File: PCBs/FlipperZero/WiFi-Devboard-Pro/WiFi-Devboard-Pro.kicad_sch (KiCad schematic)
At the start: 8 parts

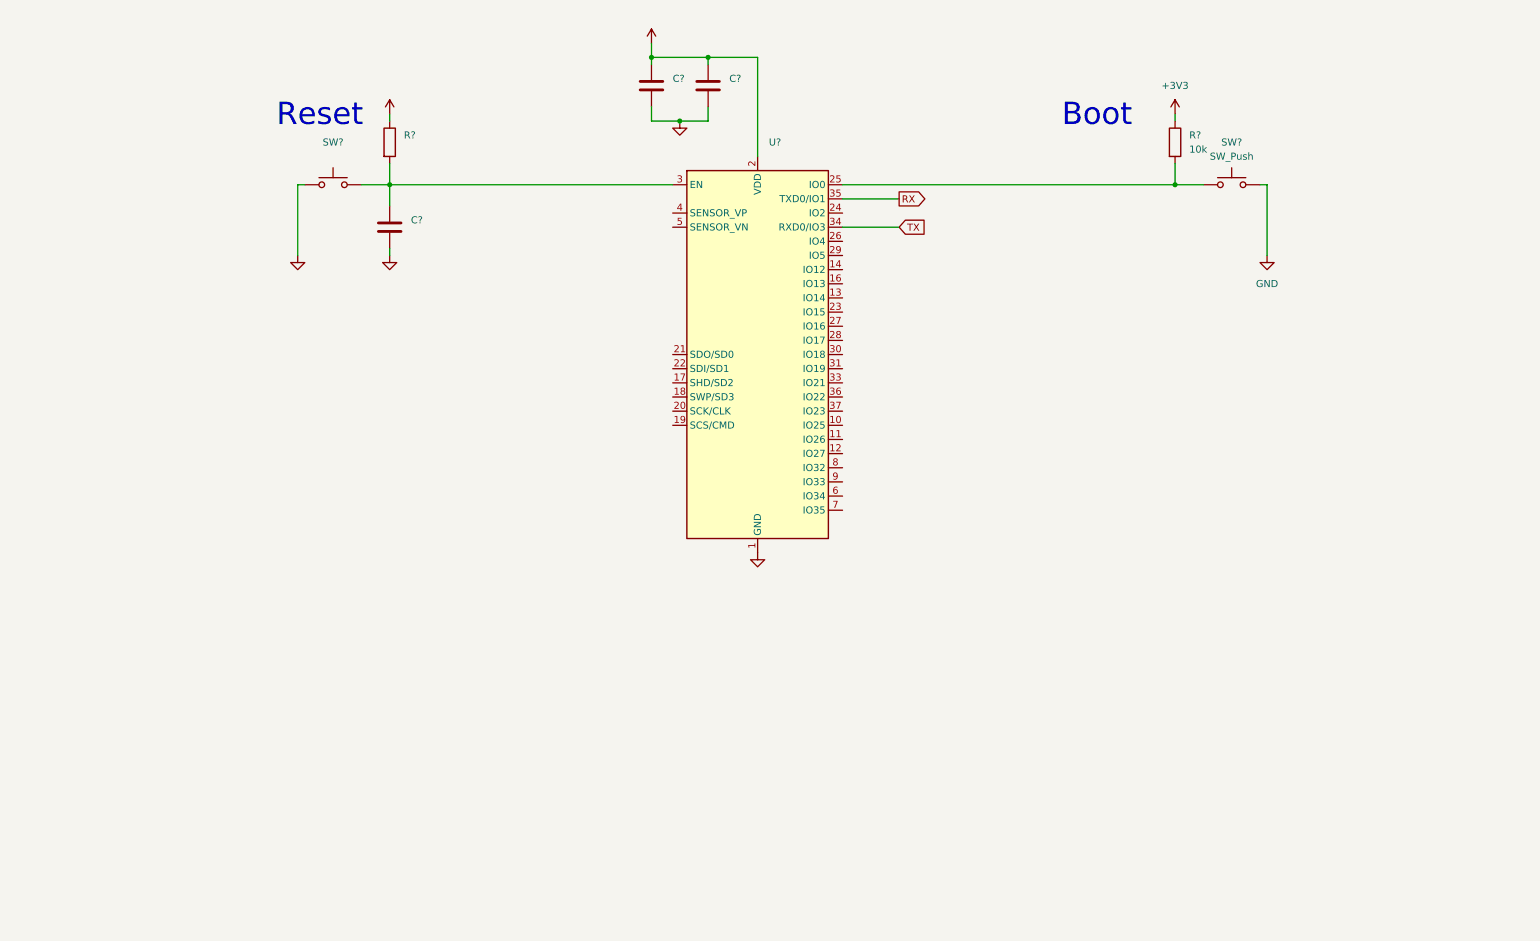
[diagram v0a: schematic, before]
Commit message: add references, edit devboard pro schematic, sd card, pin headers
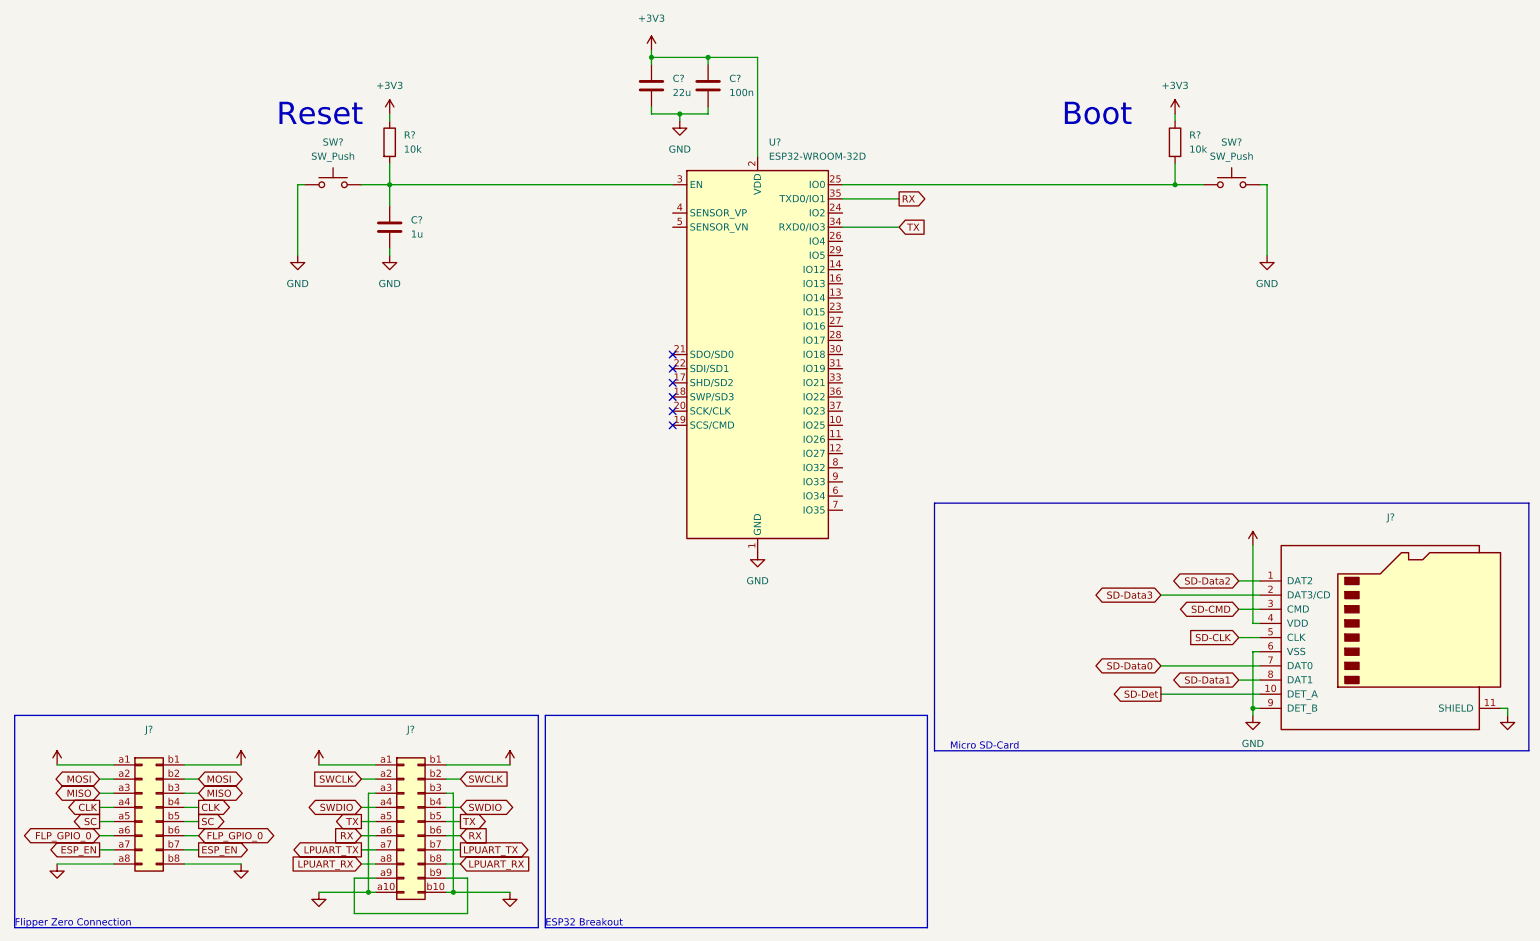
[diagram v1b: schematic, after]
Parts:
- added J?: (no value), symbol Connector_Generic:Conn_02x10_Row_Letter_First
- added J?: (no value), symbol Connector_Generic:Conn_02x08_Row_Letter_First
- added J?: (no value), symbol Connector:Micro_SD_Card_Det
- C?: value (none) -> 22u
- C?: value (none) -> 100n
- C?: value (none) -> 1u
- R?: value (none) -> 10k
- SW?: value (none) -> SW_Push
- U?: value (none) -> ESP32-WROOM-32D; footprint (none) -> RF_Module:ESP32-WROOM-32
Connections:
- net +3V3: now also J?.4 (VDD), J?.a1 (Pin_a1), J?.b1 (Pin_b1)
- net GND: now also J?.11 (SHIELD), J?.6 (VSS), J?.9 (DET_B), J?.a10 (Pin_a10), J?.a3 (Pin_a3), J?.a8 (Pin_a8), J?.b10 (Pin_b10), J?.b3 (Pin_b3), J?.b8 (Pin_b8)
- net RX: now also J?.a6 (Pin_a6), J?.b6 (Pin_b6)
- net TX: now also J?.a5 (Pin_a5), J?.b5 (Pin_b5)
- new net: J?.a9 (Pin_a9), J?.b9 (Pin_b9)
- new net +5V: J?.a1 (Pin_a1), J?.b1 (Pin_b1)
- new net CLK: J?.a4 (Pin_a4), J?.b4 (Pin_b4)
- new net ESP_EN: J?.a7 (Pin_a7), J?.b7 (Pin_b7)
- new net FLP_GPIO_0: J?.a6 (Pin_a6), J?.b6 (Pin_b6)
- new net LPUART_RX: J?.a8 (Pin_a8), J?.b8 (Pin_b8)
- new net LPUART_TX: J?.a7 (Pin_a7), J?.b7 (Pin_b7)
- new net MISO: J?.a3 (Pin_a3), J?.b3 (Pin_b3)
- new net MOSI: J?.a2 (Pin_a2), J?.b2 (Pin_b2)
- new net SC: J?.a5 (Pin_a5), J?.b5 (Pin_b5)
- new net SD-CLK: J?.5 (CLK)
- new net SD-CMD: J?.3 (CMD)
- new net SD-Data0: J?.7 (DAT0)
- new net SD-Data1: J?.8 (DAT1)
- new net SD-Data2: J?.1 (DAT2)
- new net SD-Data3: J?.2 (DAT3/CD)
- new net SD-Det: J?.10 (DET_A)
- new net SWCLK: J?.a2 (Pin_a2), J?.b2 (Pin_b2)
- new net SWDIO: J?.a4 (Pin_a4), J?.b4 (Pin_b4)
- no-connect marks 0 -> 6
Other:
- note added: "ESP32 Breakout"
- note added: "Flipper Zero Connection"
- note added: "Micro SD-Card"

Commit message: Add mosfet and transistors for power mgmt
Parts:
- added IC? (x4): DMP1045U-7, SOT96P240X120-3N, symbol SamacSys_Parts:DMP1045U-7
- added U? (x4): MMDT2907A-7-F, SOT65P210X110-6N, symbol SamacSys_Parts:MMDT2907A-7-F
- J?: value (none) -> Conn_02x10_Row_Letter_First
- J?: value (none) -> Conn_02x08_Row_Letter_First
- J?: value (none) -> Micro_SD_Card_Det; footprint (none) -> Connector_Card:microSD_HC_Hirose_DM3D-SF

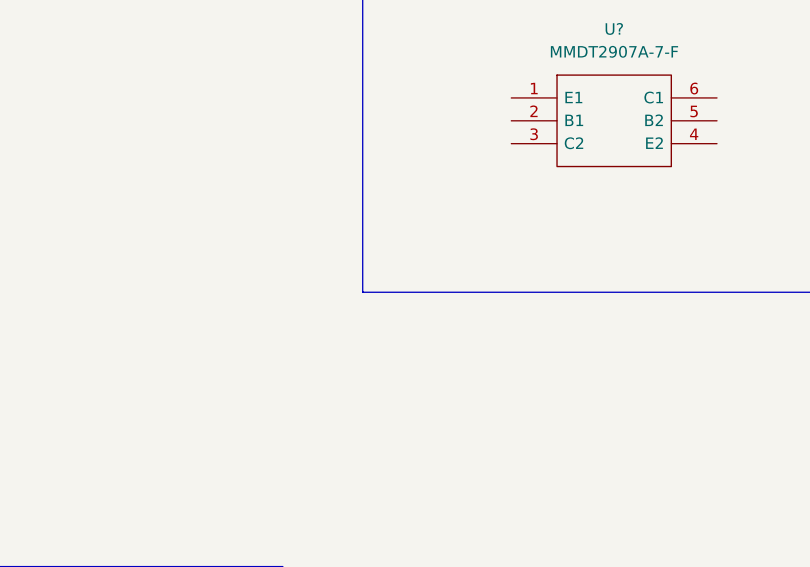
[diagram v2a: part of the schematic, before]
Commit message: Add label for power management
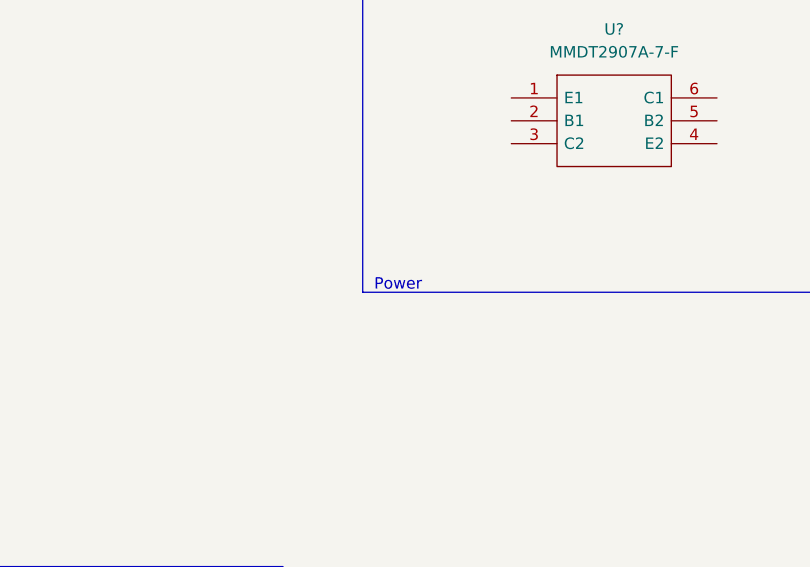
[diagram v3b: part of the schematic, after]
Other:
- note added: "Power"
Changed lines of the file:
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@@
     (effects (font (size 4 4)) (justify left bottom))
+  )
+  (text "Power" (at 294.64 90.17 0)
+    (effects (font (size 1.27 1.27)) (justify left bottom))
   )
   (text "Flipper Zero Connection" (at 12.7 196.85 0)

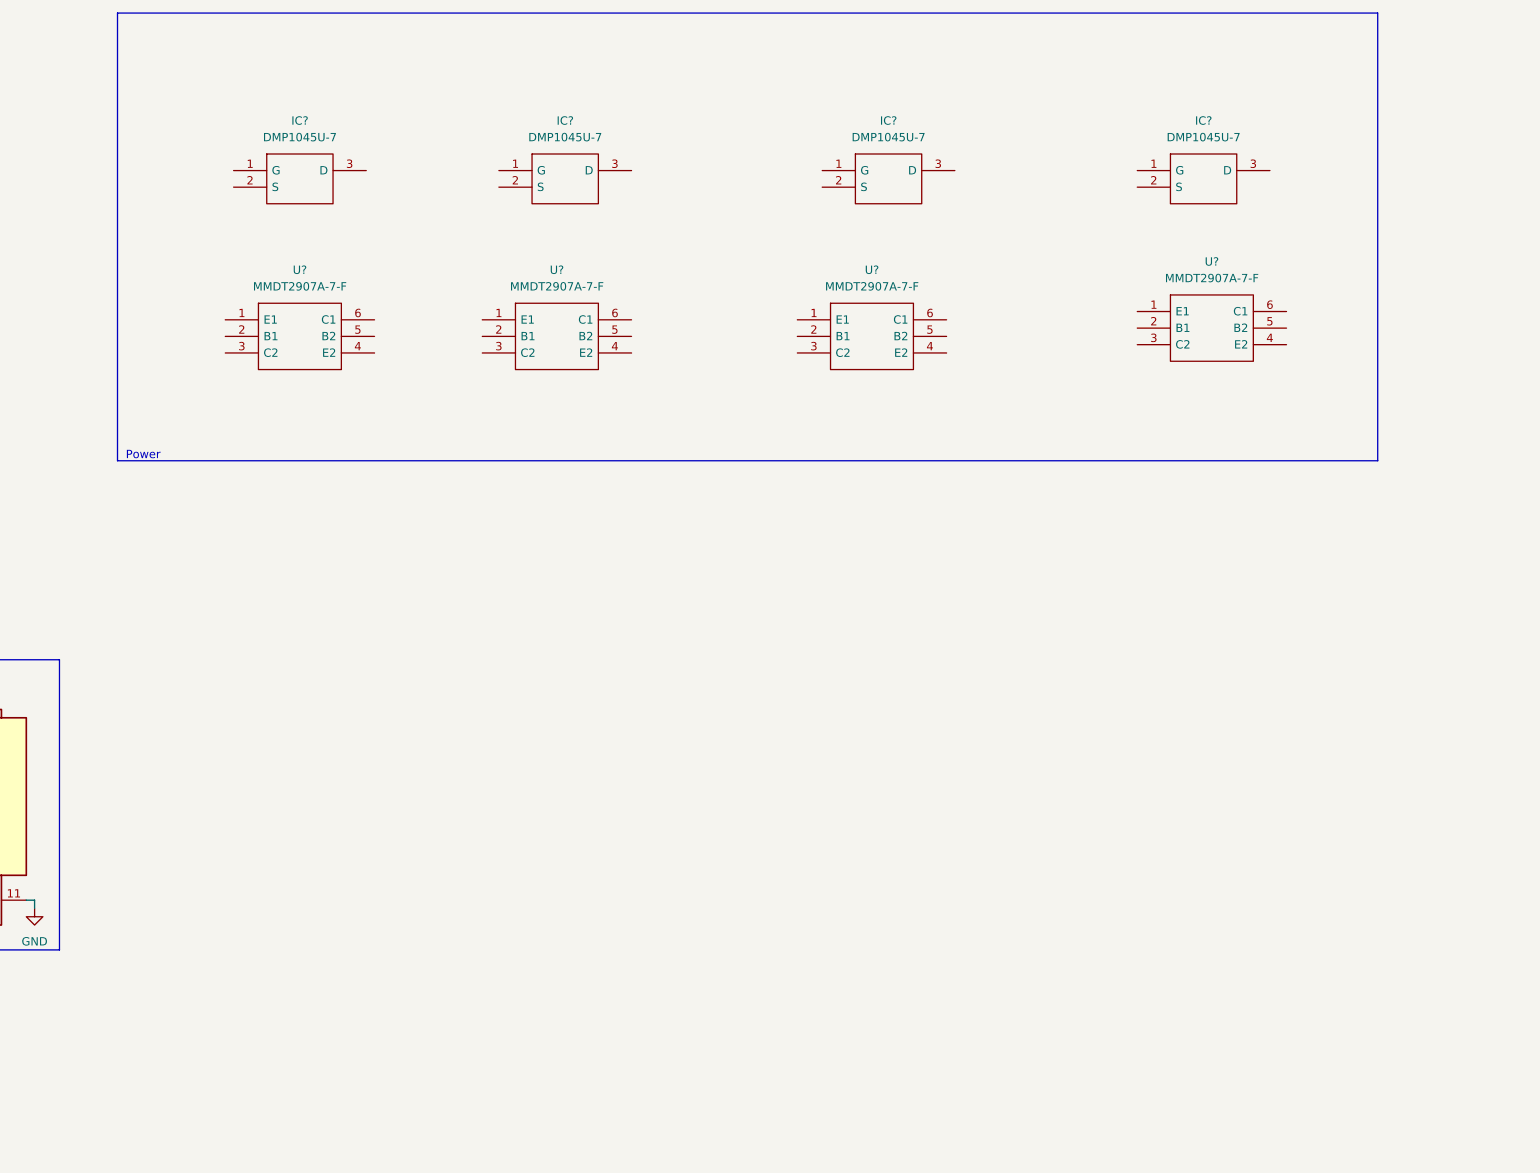
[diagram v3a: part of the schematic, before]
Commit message: Finish power mgmt circuit
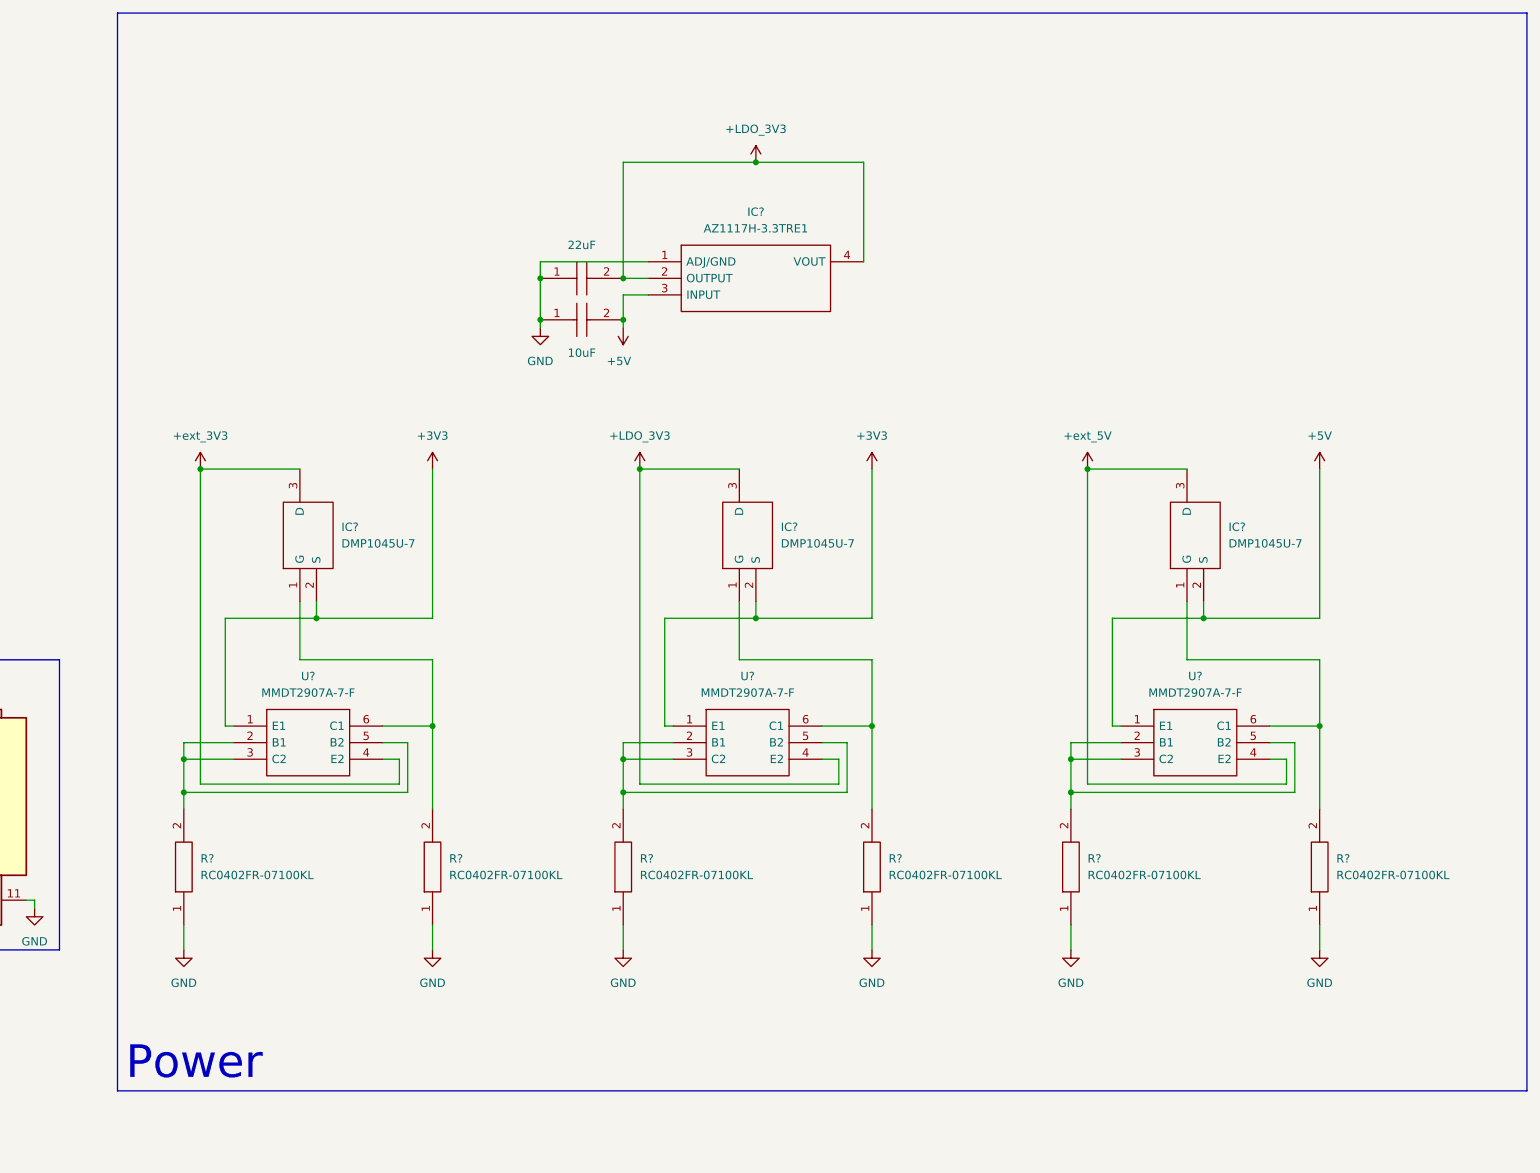
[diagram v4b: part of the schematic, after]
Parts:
- removed IC? (x3): DMP1045U-7, SOT96P240X120-3N, symbol SamacSys_Parts:DMP1045U-7
- removed U? (x3): MMDT2907A-7-F, SOT65P210X110-6N, symbol SamacSys_Parts:MMDT2907A-7-F
- added C?: 10uF, CAPC1005X70N, symbol SamacSys_Parts:CL05A106MQ5NUNC
- added C?: 22uF, CAPC1005X80N, symbol SamacSys_Parts:CM05X5R226M06AH080
- added IC? (x2): DMP1045U-7, SOT96P240X120-3N, symbol SamacSys_Parts:DMP1045U-7
- added IC?: AZ1117H-3.3TRE1, SOT230P700X180-4N, symbol SamacSys_Parts:AZ1117H-3.3TRE1
- added R? (x6): RC0402FR-07100KL, RESC1005X40N, symbol SamacSys_Parts:RC0402FR-07100KL
- added U? (x2): MMDT2907A-7-F, SOT65P210X110-6N, symbol SamacSys_Parts:MMDT2907A-7-F
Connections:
- net +3V3: now also IC?.2 (S), IC?.3 (D), U?.1 (E1), U?.4 (E2), C?.2, IC?.2 (OUTPUT), IC?.2 (S), IC?.3 (D), IC?.4 (VOUT), U?.1 (E1), U?.4 (E2)
- net +5V: now also C?.2, IC?.2 (S), IC?.3 (D), IC?.3 (INPUT), U?.1 (E1), U?.4 (E2)
- net GND: now also C?.1, C?.1, IC?.1 (ADJ/GND), R?.1, R?.1, R?.1, R?.1, R?.1, R?.1
- net at IC?.1 (G): now also U?.6 (C1), R?.2
- net at U?.2 (B1): now also U?.3 (C2), U?.5 (B2), R?.2
- new net: IC?.1 (G), R?.2, U?.6 (C1) (x2)
- new net: R?.2, U?.2 (B1), U?.3 (C2), U?.5 (B2) (x2)
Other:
- moved on the sheet: IC?, U?
